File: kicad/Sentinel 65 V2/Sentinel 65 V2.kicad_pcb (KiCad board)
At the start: 6 copper layers, 0 parts

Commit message: logo import
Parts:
- added G***: LOGO, LOGO, F.Cu at (163.7, 181.7)
- added G***: LOGO, LOGO, F.Cu at (163.6, 193.7)
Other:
- board outline added: 90.1 x 90.1 mm
- board text added: "Copyright © 2023 Kyle J Cardoza, Studio 8502. All rights reserved."
- board text added: "Designed in"
- board text added: "Released under the CERN Open Hardware License, Version 2 (Permissive — CERN-OHL-P)"

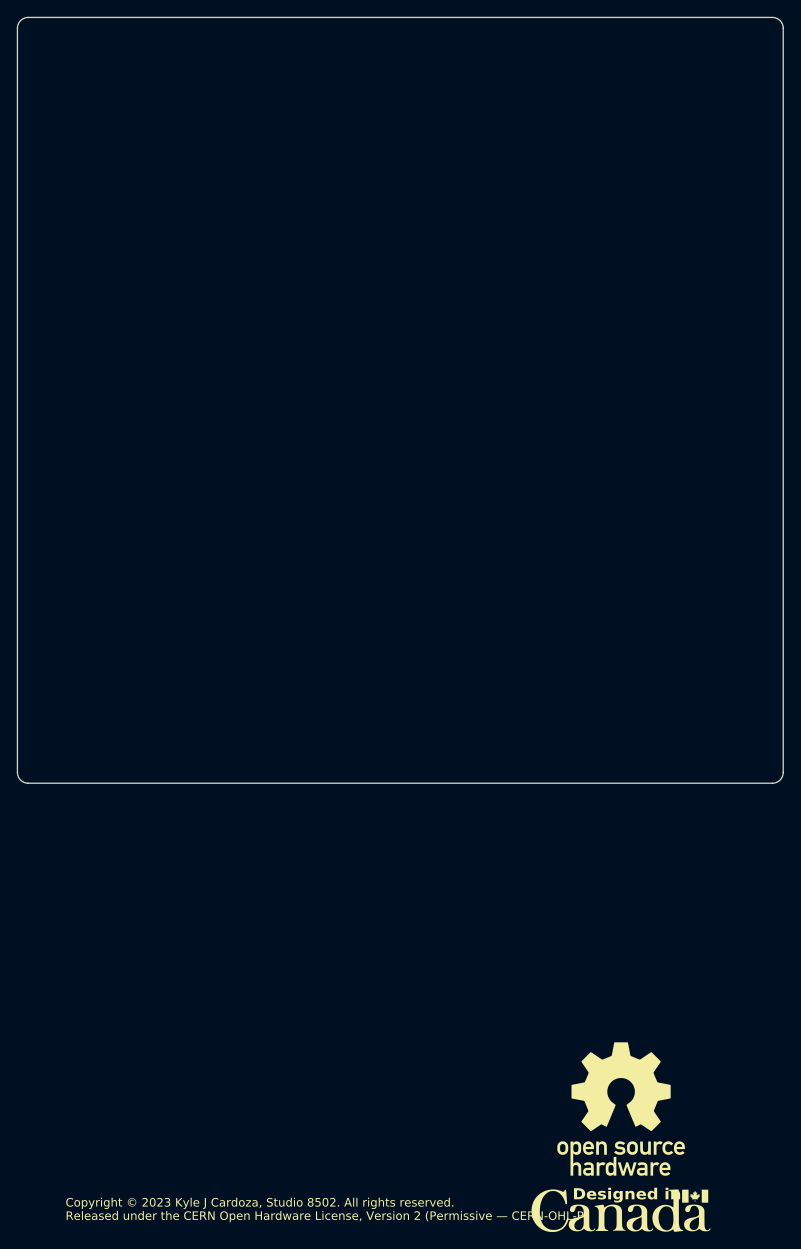
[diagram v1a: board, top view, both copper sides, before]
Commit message: Updated schematic PDF
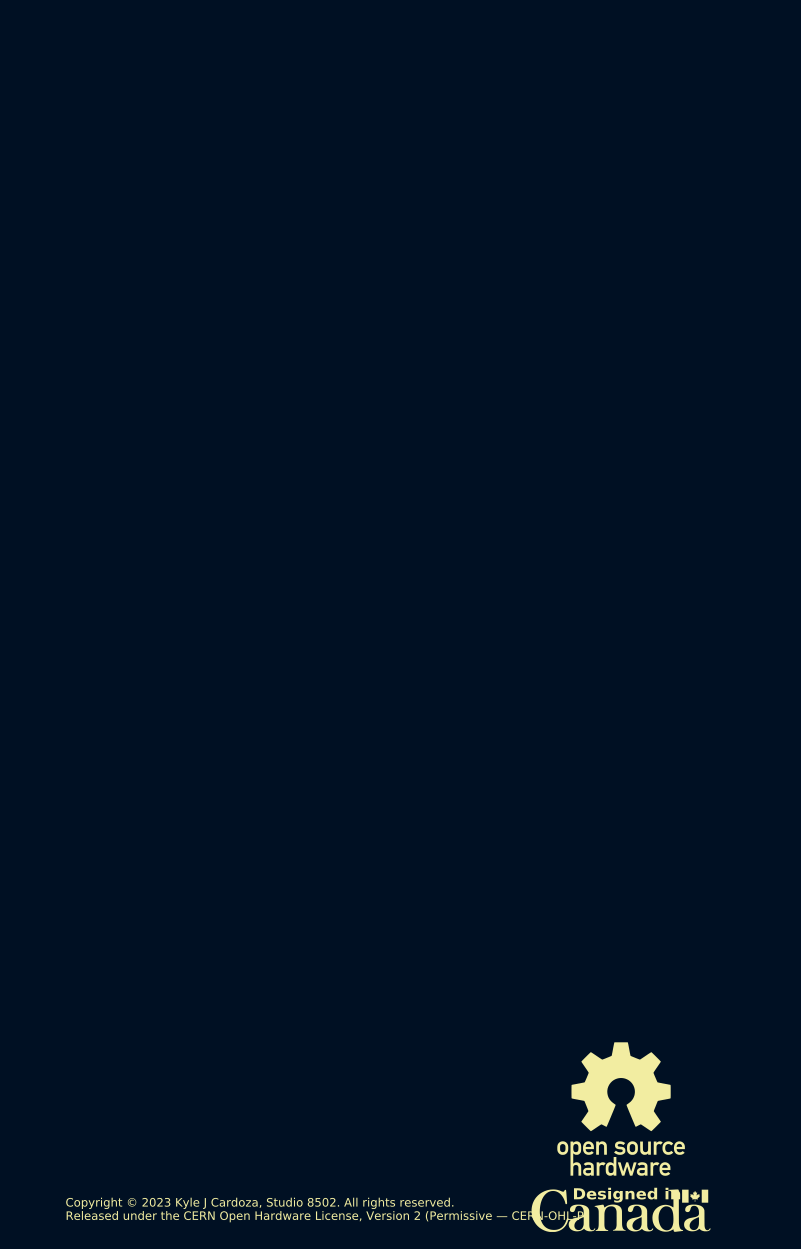
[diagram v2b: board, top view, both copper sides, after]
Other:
- board outline removed
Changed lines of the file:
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@@
   (paper "A4")
   (layers
-    (0 "F.Cu" signal "F.Cu.BRK")
+    (0 "F.Cu" signal "F.Cu.Breakout")
     (1 "In1.Cu" power "In1.Cu.GND")
     (2 "In2.Cu" signal "In2.Cu.Vertical")
@@
       (stroke (width 0) (type solid)) (fill solid) (layer "F.SilkS"))
   )
-  (gr_arc locked (start 182.77 142.13) (mid 182.398026 143.028026) (end 181.5 143.4)
-    (stroke (width 0.1) (type default)) (layer "Edge.Cuts"))
-  (gr_line locked (start 182.77 54.61) (end 182.77 142.13)
-    (stroke (width 0.1) (type default)) (layer "Edge.Cuts"))
-  (gr_line locked (start 92.71 142.13) (end 92.71 54.61)
-    (stroke (width 0.1) (type default)) (layer "Edge.Cuts"))
-  (gr_arc locked (start 93.98 143.4) (mid 93.081974 143.028026) (end 92.71 142.13)
-    (stroke (width 0.1) (type default)) (layer "Edge.Cuts"))
-  (gr_arc locked (start 92.71 54.61) (mid 93.081974 53.711974) (end 93.98 53.34)
-    (stroke (width 0.1) (type default)) (layer "Edge.Cuts"))
-  (gr_arc locked (start 181.5 53.34) (mid 182.398026 53.711974) (end 182.77 54.61)
-    (stroke (width 0.1) (type default)) (layer "Edge.Cuts"))
-  (gr_line locked (start 93.98 53.34) (end 181.5 53.34)
-    (stroke (width 0.1) (type default)) (layer "Edge.Cuts"))
-  (gr_line locked (start 181.5 143.4) (end 93.98 143.4)
-    (stroke (width 0.1) (type default)) (layer "Edge.Cuts"))
   (gr_text "Copyright © 2023 Kyle J Cardoza, Studio 8502. All rights reserved." (at 98.365178 193.308829) (layer "F.SilkS")
     (effects (font (face "Baskerville") (size 1 1) (thickness 0.15)) (justify left bottom))

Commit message: Updated license terms
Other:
- board text added: "Licensed under CERN-OHL-P v2"
- board text removed: "Released under the CERN Open Hardware License, Version 2 (Permissive — CERN-OHL-P)"
